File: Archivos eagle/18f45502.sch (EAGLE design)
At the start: 27 parts, among them IC1 PIC18F4550_40, IC2 7805DT, Q1 20MHz, X1 DCJ0202, X2 PN61729-S

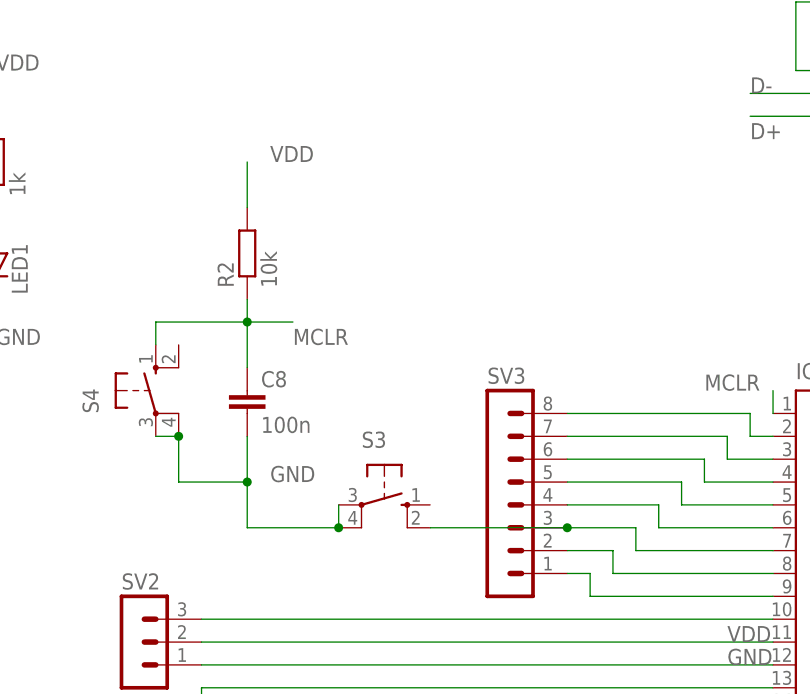
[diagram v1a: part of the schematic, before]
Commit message: build alpha 1.5.1
se agrego una resistencia de pull up en el pulsador de bootloader (super
importante)
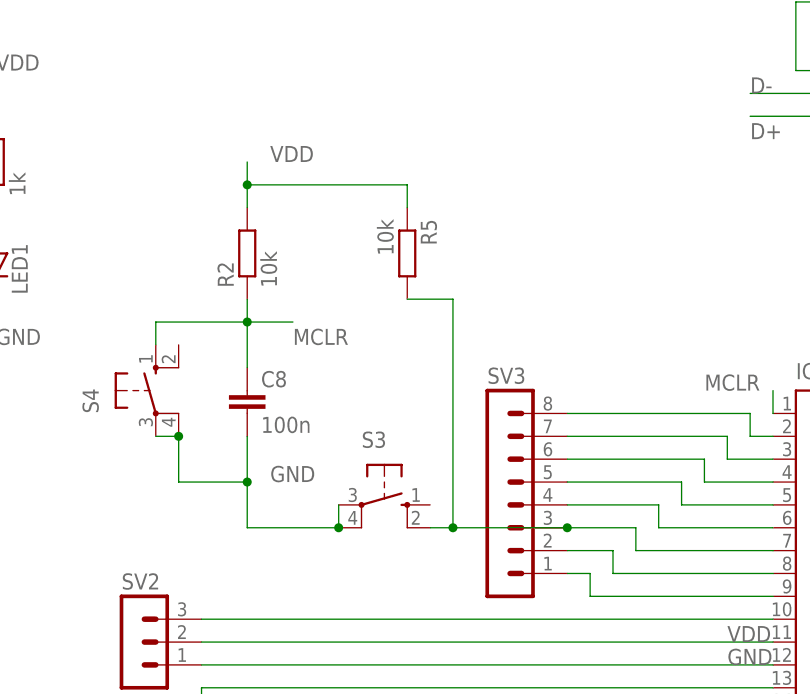
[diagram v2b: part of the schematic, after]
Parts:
- added R5: 10k, resistor:R-EU_R0805
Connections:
- net N$18: now also R5.2
- net VDD: now also R5.1
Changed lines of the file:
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@@
 <part name="C1" library="resistor" deviceset="C-EU" device="C0805K" value=".1uF"/>
 <part name="C2" library="resistor" deviceset="C-EU" device="C0805K" value=".33uF"/>
+<part name="R5" library="resistor" deviceset="R-EU_" device="R0805" value="10k"/>
 </parts>
 <sheets>
@@
 <instance part="C1" gate="G$1" x="129.54" y="127"/>
 <instance part="C2" gate="G$1" x="99.06" y="124.46" rot="R180"/>
+<instance part="R5" gate="G$1" x="-12.7" y="101.6" rot="R270"/>
 </instances>
 <busses>
@@
 </segment>
 <segment>
-<wire x1="-30.48" y1="106.68" x2="-30.48" y2="111.76" width="0.1524" layer="91"/>
+<wire x1="-30.48" y1="106.68" x2="-30.48" y2="109.22" width="0.1524" layer="91"/>
 <label x="-27.94" y="111.76" size="1.778" layer="95"/>
 <pinref part="R2" gate="G$1" pin="2"/>
+<pinref part="R5" gate="G$1" pin="1"/>
+<wire x1="-30.48" y1="109.22" x2="-30.48" y2="111.76" width="0.1524" layer="91"/>
+<wire x1="-12.7" y1="106.68" x2="-12.7" y2="109.22" width="0.1524" layer="91"/>
+<wire x1="-12.7" y1="109.22" x2="-30.48" y2="109.22" width="0.1524" layer="91"/>
+<junction x="-30.48" y="109.22"/>
 </segment>
 <segment>
@@
 <wire x1="12.7" y1="68.58" x2="12.7" y2="71.12" width="0.1524" layer="91"/>
 <wire x1="12.7" y1="71.12" x2="5.08" y2="71.12" width="0.1524" layer="91"/>
-<wire x1="-10.16" y1="71.12" x2="5.08" y2="71.12" width="0.1524" layer="91"/>
+<wire x1="-10.16" y1="71.12" x2="-7.62" y2="71.12" width="0.1524" layer="91"/>
 <junction x="5.08" y="71.12"/>
 <pinref part="IC1" gate="G$1" pin="RA5/AN4/!SS!/HLVDIN/C2OUT"/>
 <pinref part="SV3" gate="1" pin="3"/>
 <pinref part="S3" gate="1" pin="S1"/>
-</segment>
-</net>
+<pinref part="R5" gate="G$1" pin="2"/>
+<wire x1="-7.62" y1="71.12" x2="5.08" y2="71.12" width="0.1524" layer="91"/>
+<wire x1="-12.7" y1="96.52" x2="-7.62" y2="96.52" width="0.1524" layer="91"/>
+<wire x1="-7.62" y1="96.52" x2="-7.62" y2="71.12" width="0.1524" layer="91"/>
+<junction x="-7.62" y="71.12"/>
+</segment>
+</net>
